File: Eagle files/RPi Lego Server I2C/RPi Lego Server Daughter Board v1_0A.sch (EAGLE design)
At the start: 21 parts, among them Q1 16MHz, Q2 MOSFET-NCHANNEL2N7000

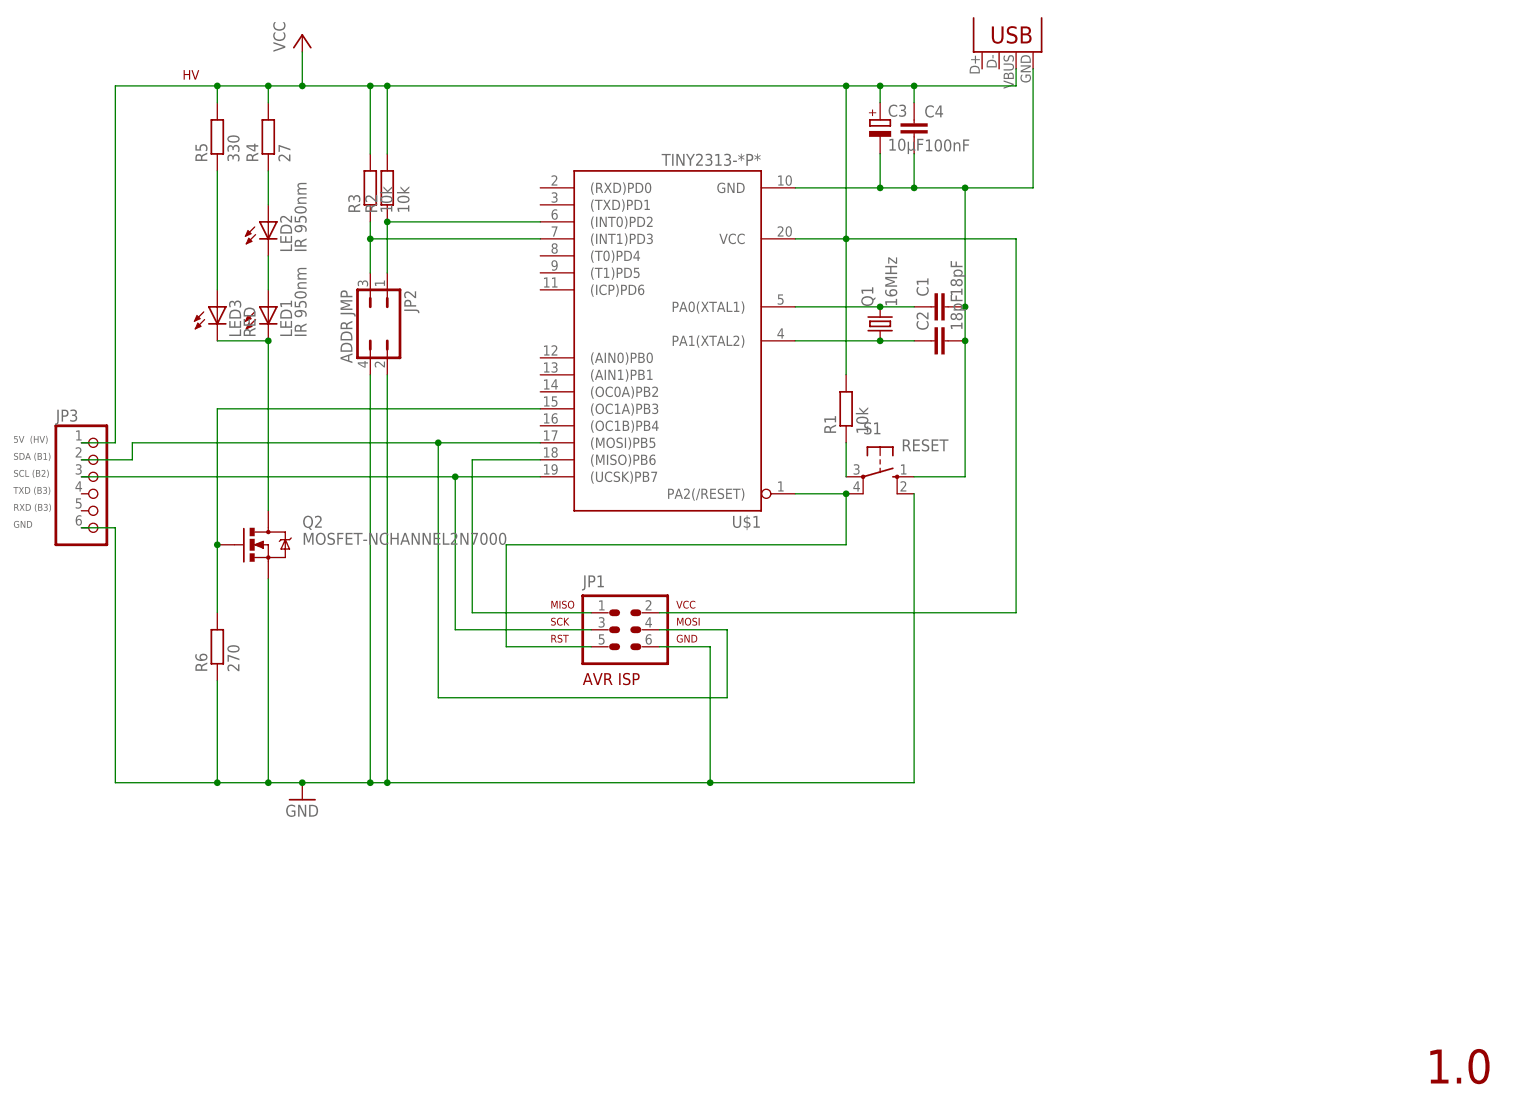
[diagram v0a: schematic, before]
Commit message: Uploaded new schematics, both interconnect board and IR board. USB connector (for power) has been moved to interconnect board. Also added routed PCB designs
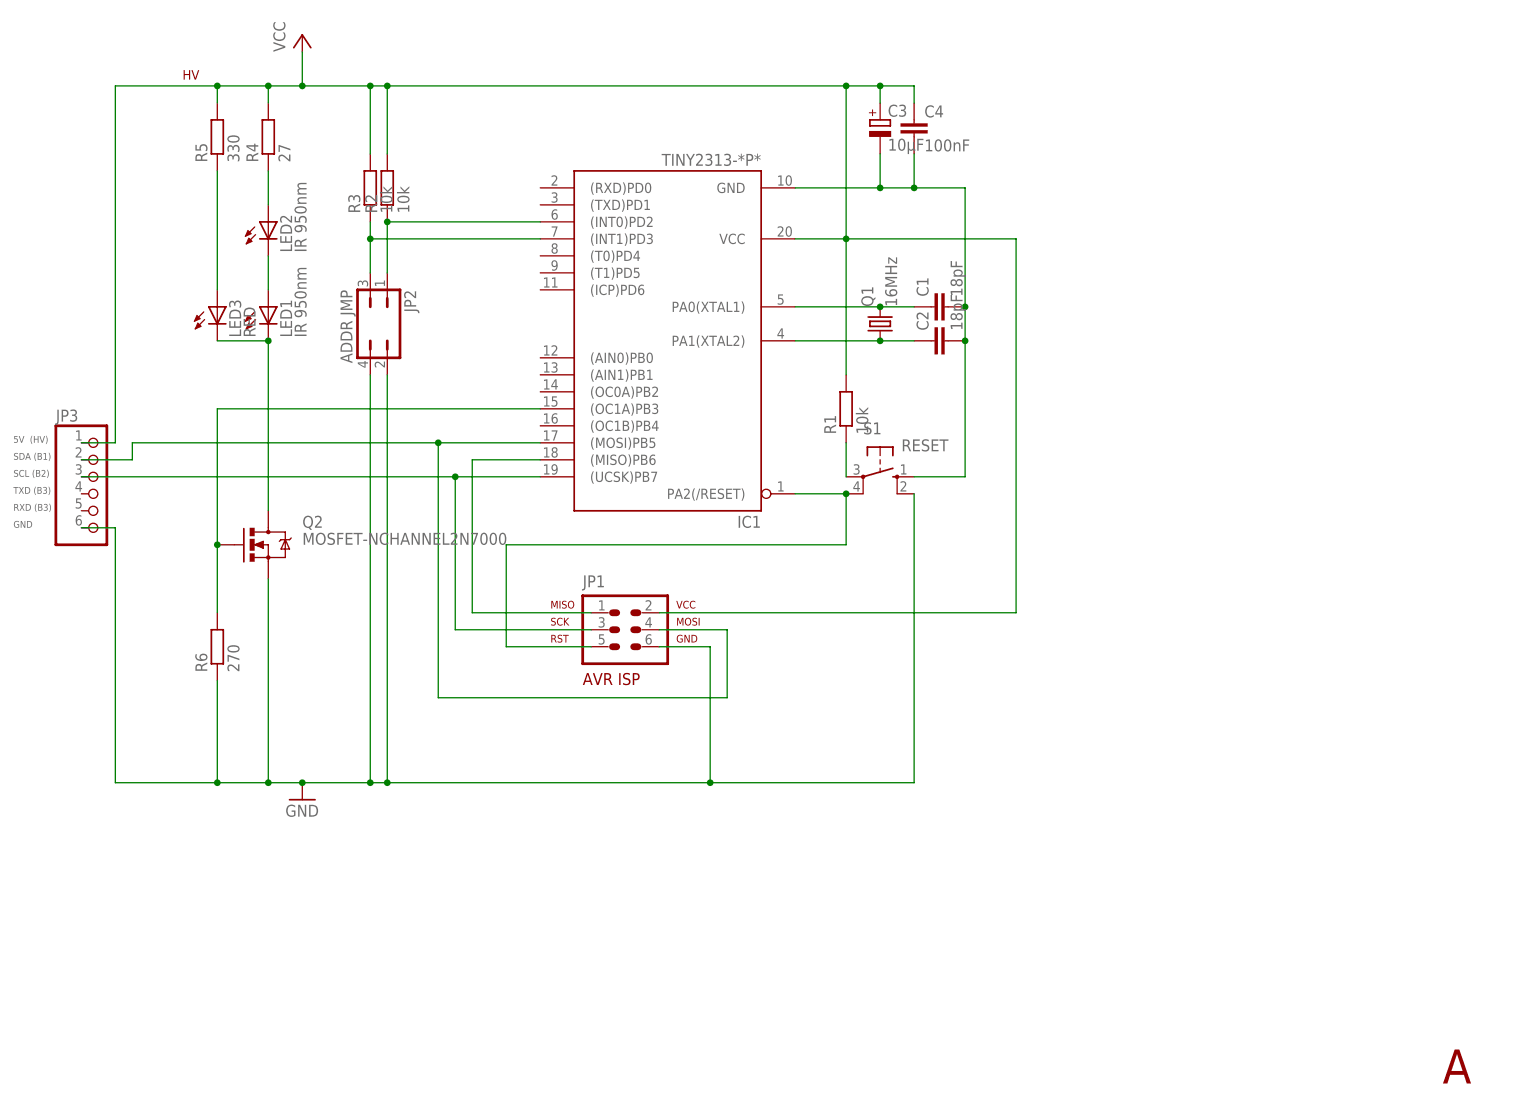
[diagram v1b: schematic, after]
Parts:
- removed JP4: USB-B, SparkFun-Connectors:USBPTH
- renumbered U$1 to IC1
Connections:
- net GND: no longer JP4.GND
- net VCC: no longer JP4.VBUS
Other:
- note added: "A"
- note removed: "1.0"
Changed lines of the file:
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@@
 </variantdefs>
 <classes>
-<class number="0" name="default" width="0" drill="0">
+<class number="0" name="default" width="0" drill="0.6096">
 </class>
 </classes>
 <parts>
 <part name="FRAME1" library="frames" deviceset="DINA4_L" device=""/>
-<part name="U$1" library="avr-7" deviceset="TINY2313*" device="-*P*"/>
+<part name="IC1" library="avr-7" deviceset="TINY2313*" device="-*P*"/>
 <part name="P+1" library="supply1" deviceset="VCC" device=""/>
 <part name="GND1" library="supply1" deviceset="GND" device=""/>
@@
 <part name="R6" library="resistor" deviceset="R-EU_" device="0207_10" value="270"/>
 <part name="JP3" library="pinhead" deviceset="PINHD-1X6" device=""/>
-<part name="JP4" library="SparkFun-Connectors" deviceset="USB" device="PTH" value="USB-B"/>
 <part name="C3" library="rcl" deviceset="CPOL-EU" device="E2.5-6" value="10µF"/>
 <part name="C4" library="rcl" deviceset="C-EU" device="050-030X075" value="100nF"/>
@@
 <sheet>
 <plain>
-<text x="216.154" y="-9.398" size="5.08" layer="94">1.0</text>
+<text x="218.694" y="-9.398" size="5.08" layer="94">A</text>
 <rectangle x1="131.2799" y1="9.1567" x2="131.5085" y2="9.1821" layer="200"/>
 <rectangle x1="131.8895" y1="9.1567" x2="132.1181" y2="9.1821" layer="200"/>
@@
 <instance part="FRAME1" gate="G$1" x="-35.56" y="-15.24"/>
 <instance part="FRAME1" gate="G$2" x="127" y="-15.24"/>
-<instance part="U$1" gate="G$1" x="101.6" y="96.52" rot="R180"/>
+<instance part="IC1" gate="G$1" x="101.6" y="96.52" rot="R180"/>
 <instance part="P+1" gate="VCC" x="48.26" y="147.32"/>
 <instance part="GND1" gate="1" x="48.26" y="33.02"/>
@@
 <instance part="R6" gate="G$1" x="35.56" y="55.88" rot="R90"/>
 <instance part="JP3" gate="A" x="17.78" y="78.74"/>
-<instance part="JP4" gate="G$1" x="157.48" y="144.78" rot="R90"/>
 <instance part="C3" gate="G$1" x="134.62" y="134.62"/>
 <instance part="C4" gate="G$1" x="139.7" y="134.62"/>
@@
 <wire x1="60.96" y1="139.7" x2="129.54" y2="139.7" width="0.1524" layer="91"/>
 <wire x1="129.54" y1="139.7" x2="129.54" y2="116.84" width="0.1524" layer="91"/>
-<pinref part="U$1" gate="G$1" pin="VCC"/>
+<pinref part="IC1" gate="G$1" pin="VCC"/>
 <wire x1="129.54" y1="116.84" x2="121.92" y2="116.84" width="0.1524" layer="91"/>
 <junction x="129.54" y="116.84"/>
@@
 <junction x="129.54" y="139.7"/>
 <wire x1="129.54" y1="139.7" x2="134.62" y2="139.7" width="0.1524" layer="91"/>
-<pinref part="JP4" gate="G$1" pin="VBUS"/>
 <wire x1="134.62" y1="139.7" x2="139.7" y2="139.7" width="0.1524" layer="91"/>
-<wire x1="139.7" y1="139.7" x2="154.94" y2="139.7" width="0.1524" layer="91"/>
-<wire x1="154.94" y1="139.7" x2="154.94" y2="142.24" width="0.1524" layer="91"/>
 <junction x="134.62" y="139.7"/>
-<junction x="139.7" y="139.7"/>
 <pinref part="C3" gate="G$1" pin="+"/>
 <wire x1="134.62" y1="137.16" x2="134.62" y2="139.7" width="0.1524" layer="91"/>
@@
 <wire x1="78.74" y1="55.88" x2="78.74" y2="71.12" width="0.1524" layer="91"/>
 <wire x1="78.74" y1="71.12" x2="129.54" y2="71.12" width="0.1524" layer="91"/>
-<pinref part="U$1" gate="G$1" pin="PA2(/RESET)"/>
+<pinref part="IC1" gate="G$1" pin="PA2(/RESET)"/>
 <pinref part="S1" gate="1" pin="P1"/>
 <wire x1="121.92" y1="78.74" x2="129.54" y2="78.74" width="0.1524" layer="91"/>
@@
 <wire x1="139.7" y1="81.28" x2="147.32" y2="81.28" width="0.1524" layer="91"/>
 <wire x1="147.32" y1="81.28" x2="147.32" y2="101.6" width="0.1524" layer="91"/>
-<pinref part="U$1" gate="G$1" pin="GND"/>
+<pinref part="IC1" gate="G$1" pin="GND"/>
 <wire x1="147.32" y1="101.6" x2="147.32" y2="106.68" width="0.1524" layer="91"/>
 <wire x1="147.32" y1="106.68" x2="147.32" y2="124.46" width="0.1524" layer="91"/>
@@
 <pinref part="C2" gate="G$1" pin="2"/>
 <junction x="147.32" y="101.6"/>
-<junction x="147.32" y="124.46"/>
-<pinref part="JP4" gate="G$1" pin="GND"/>
 <wire x1="139.7" y1="124.46" x2="134.62" y2="124.46" width="0.1524" layer="91"/>
 <wire x1="134.62" y1="124.46" x2="121.92" y2="124.46" width="0.1524" layer="91"/>
-<wire x1="157.48" y1="142.24" x2="157.48" y2="124.46" width="0.1524" layer="91"/>
-<wire x1="157.48" y1="124.46" x2="147.32" y2="124.46" width="0.1524" layer="91"/>
 <junction x="139.7" y="124.46"/>
 <junction x="134.62" y="124.46"/>
@@
 <net name="XTAL2" class="0">
 <segment>
-<pinref part="U$1" gate="G$1" pin="PA0(XTAL1)"/>
+<pinref part="IC1" gate="G$1" pin="PA0(XTAL1)"/>
 <pinref part="C1" gate="G$1" pin="1"/>
 <wire x1="121.92" y1="106.68" x2="134.62" y2="106.68" width="0.1524" layer="91"/>
@@
 <net name="XTAL1" class="0">
 <segment>
-<pinref part="U$1" gate="G$1" pin="PA1(XTAL2)"/>
+<pinref part="IC1" gate="G$1" pin="PA1(XTAL2)"/>
 <pinref part="C2" gate="G$1" pin="1"/>
 <wire x1="121.92" y1="101.6" x2="134.62" y2="101.6" width="0.1524" layer="91"/>
@@
 <wire x1="91.44" y1="60.96" x2="73.66" y2="60.96" width="0.1524" layer="91"/>
 <wire x1="73.66" y1="60.96" x2="73.66" y2="83.82" width="0.1524" layer="91"/>
-<pinref part="U$1" gate="G$1" pin="(MISO)PB6"/>
+<pinref part="IC1" gate="G$1" pin="(MISO)PB6"/>
 <wire x1="73.66" y1="83.82" x2="83.82" y2="83.82" width="0.1524" layer="91"/>
 </segment>
@@
 <wire x1="91.44" y1="58.42" x2="71.12" y2="58.42" width="0.1524" layer="91"/>
 <wire x1="71.12" y1="58.42" x2="71.12" y2="81.28" width="0.1524" layer="91"/>
-<pinref part="U$1" gate="G$1" pin="(UCSK)PB7"/>
+<pinref part="IC1" gate="G$1" pin="(UCSK)PB7"/>
 <wire x1="71.12" y1="81.28" x2="83.82" y2="81.28" width="0.1524" layer="91"/>
 <junction x="71.12" y="81.28"/>
@@
 <wire x1="111.76" y1="48.26" x2="68.58" y2="48.26" width="0.1524" layer="91"/>
 <wire x1="68.58" y1="48.26" x2="68.58" y2="86.36" width="0.1524" layer="91"/>
-<pinref part="U$1" gate="G$1" pin="(MOSI)PB5"/>
+<pinref part="IC1" gate="G$1" pin="(MOSI)PB5"/>
 <wire x1="68.58" y1="86.36" x2="83.82" y2="86.36" width="0.1524" layer="91"/>
 <junction x="68.58" y="86.36"/>
@@
 <segment>
 <pinref part="R2" gate="G$1" pin="1"/>
-<pinref part="U$1" gate="G$1" pin="(INT0)PD2"/>
+<pinref part="IC1" gate="G$1" pin="(INT0)PD2"/>
 <wire x1="60.96" y1="119.38" x2="83.82" y2="119.38" width="0.1524" layer="91"/>
 <junction x="60.96" y="119.38"/>
@@
 <pinref part="R3" gate="G$1" pin="1"/>
 <wire x1="58.42" y1="119.38" x2="58.42" y2="116.84" width="0.1524" layer="91"/>
-<pinref part="U$1" gate="G$1" pin="(INT1)PD3"/>
+<pinref part="IC1" gate="G$1" pin="(INT1)PD3"/>
 <wire x1="58.42" y1="116.84" x2="83.82" y2="116.84" width="0.1524" layer="91"/>
 <junction x="58.42" y="116.84"/>
@@
 <net name="N$17" class="0">
 <segment>
-<pinref part="U$1" gate="G$1" pin="(OC1A)PB3"/>
+<pinref part="IC1" gate="G$1" pin="(OC1A)PB3"/>
 <wire x1="83.82" y1="91.44" x2="35.56" y2="91.44" width="0.1524" layer="91"/>
 <pinref part="Q2" gate="G$1" pin="G"/>
